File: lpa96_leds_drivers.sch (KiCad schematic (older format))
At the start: 115 parts, among them U3 TLC5941, U4 TLC5941, U5 TLC5941, U6 TLC5941, U7 TLC5941, U8 TLC5941

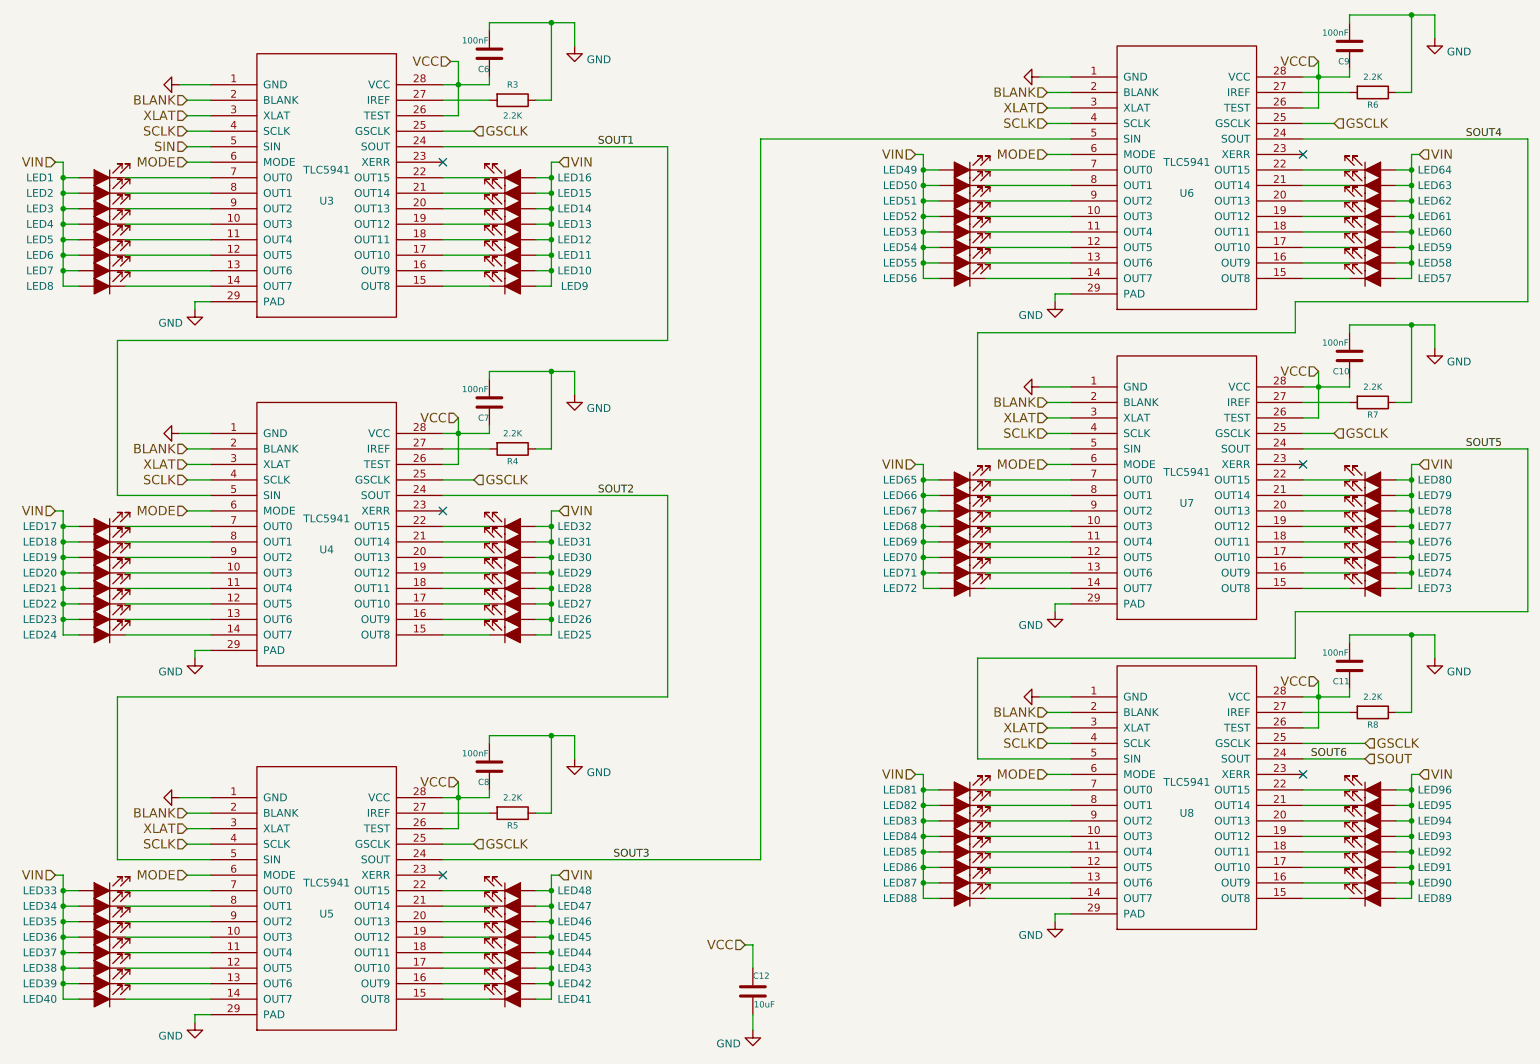
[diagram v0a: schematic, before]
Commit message: fix ERC errors, added last 3d model, other misc
changed TLC5941 pin29 pad to 'passive' type to fix ERC error
added PWR_FLAG special symbol on to input GND to fix ERC error
changed all VCC to proper power symbol instead of net alias
connected shield tabs of SDCARD footprint to GND (symbol doesn't have a pin)
changed SD_CARD symbol for pin8/9 are passive instead of NC (avoids ERCs)
changed name of pin8/9 from "RSV" to DAT1/DAT2 to match datasheet of guessed part
changed pin4 of regulator back to VCC (got messed up after change to VCC power symbols instead of net alias
added 3d model to P1 (revise after BOM received)
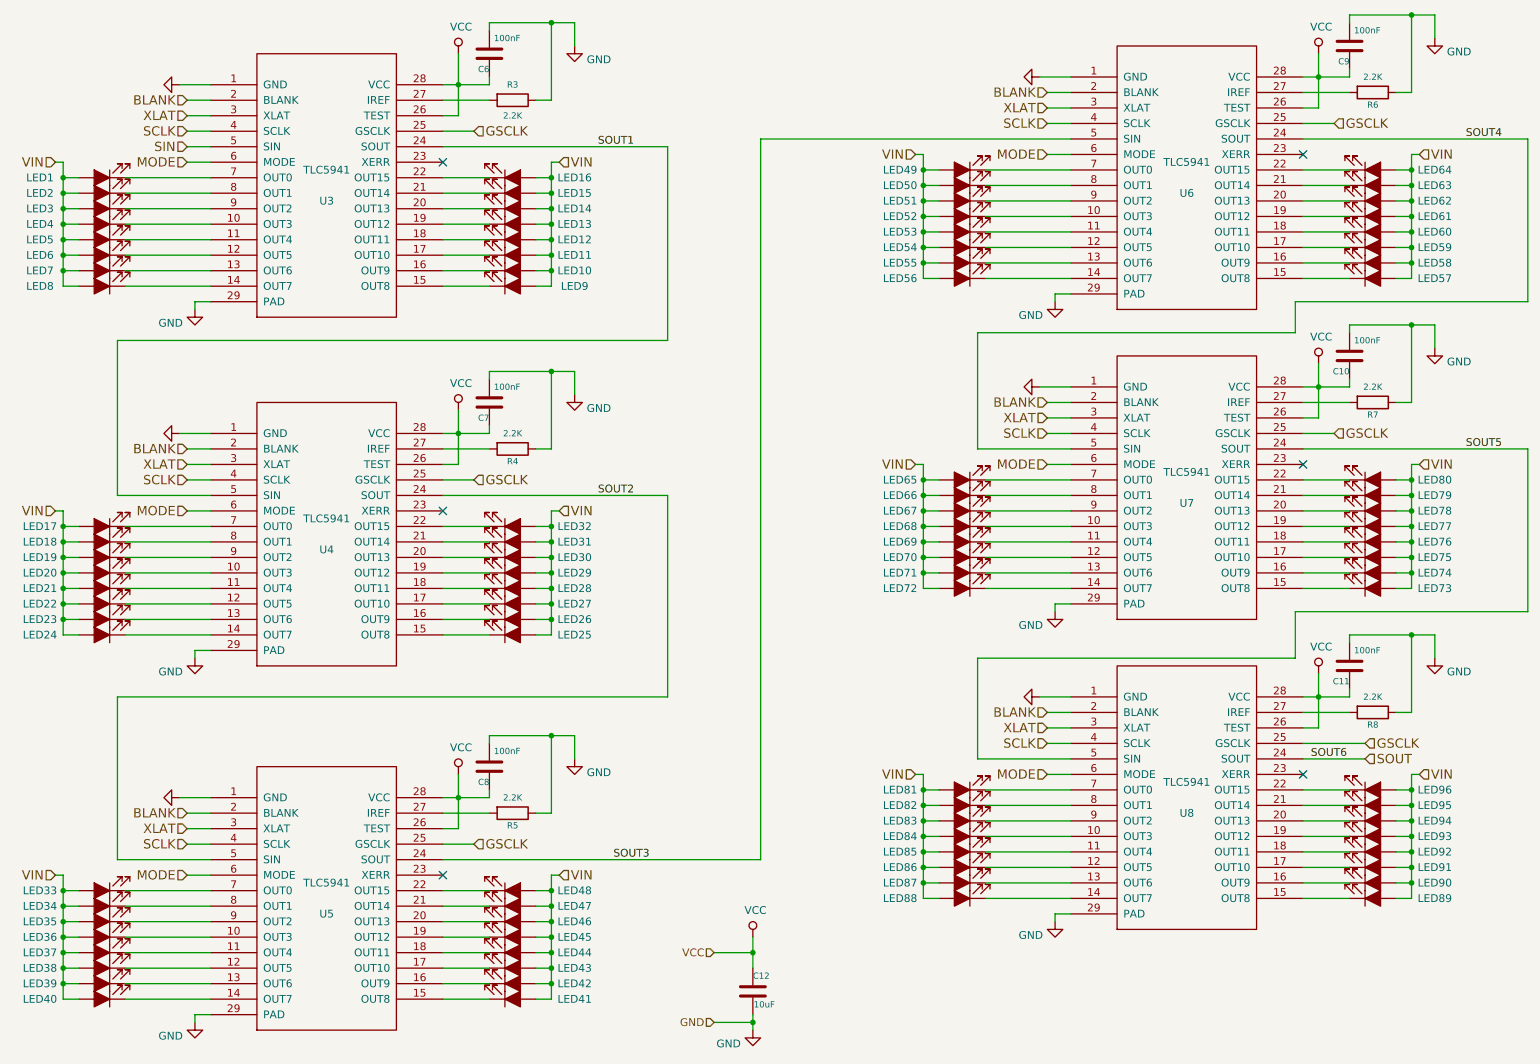
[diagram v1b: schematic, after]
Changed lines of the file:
@@
 EESchema Schematic File Version 4
-LIBS:tca-cache
+LIBS:lpa96-cache
 EELAYER 30 0
 EELAYER END
@@
 Connection ~ 3850 5600
 Wire Wire Line
-	3850 5500 3850 5600
-Wire Wire Line
 	3850 5800 3750 5800
 Wire Wire Line
@@
 	5200 1400 3750 1400
 Connection ~ 3850 3250
-Wire Wire Line
-	3850 3150 3850 3250
 Wire Wire Line
 	3850 3450 3750 3450
@@
 $EndComp
 $Comp
-L Device:C C8
-U 1 1 53630180
-P 4050 5400
-F 0 "C8" H 4050 5500 40  0000 L CNN
-F 1 "100nF" H 4056 5315 40  0000 L CNN
-F 2 "Capacitors_SMD:C_0805" H 4088 5250 30  0001 C CNN
-F 3 "~" H 4050 5400 60  0000 C CNN
-	1    4050 5400
-	-1   0    0    1
-$EndComp
-$Comp
 L lpa96_symbols:TLC5941 U4
 U 1 1 536301A0
@@
 	0    1    1    0
 $EndComp
-$Comp
-L Device:C C7
-U 1 1 53AA0807
-P 4050 3050
-F 0 "C7" H 4050 3150 40  0000 L CNN
-F 1 "100nF" H 4056 2965 40  0000 L CNN
-F 2 "Capacitors_SMD:C_0805" H 4088 2900 30  0001 C CNN
-F 3 "~" H 4050 3050 60  0000 C CNN
-	1    4050 3050
-	-1   0    0    1
-$EndComp
 NoConn ~ 3750 1500
 $Comp
@@
 $EndComp
 $Comp
-L Device:C C6
-U 1 1 53630972
-P 4050 800
-F 0 "C6" H 4050 900 40  0000 L CNN
-F 1 "100nF" H 4056 715 40  0000 L CNN
-F 2 "Capacitors_SMD:C_0805" H 4088 650 30  0001 C CNN
-F 3 "~" H 4050 800 60  0000 C CNN
-	1    4050 800
-	-1   0    0    1
-$EndComp
-$Comp
 L lpa96_symbols:TLC5941 U3
 U 1 1 53630973
@@
 Text HLabel 3950 5900 2    60   Input ~ 0
 GSCLK
-Text HLabel 3850 5500 0    60   Input ~ 0
-VCC
-Text HLabel 3850 3150 0    60   Input ~ 0
-VCC
 Text HLabel 4500 1500 2    60   Input ~ 0
 VIN
-Text HLabel 3800 850  0    60   Input ~ 0
-VCC
 Text HLabel 1250 1500 0    60   Input ~ 0
 VIN
@@
 Connection ~ 9400 4950
 Wire Wire Line
-	9400 4850 9400 4950
-Wire Wire Line
 	9400 5150 9300 5150
 Wire Wire Line
@@
 	9400 1150 9300 1150
 Connection ~ 9400 950
-Wire Wire Line
-	9400 850  9400 950
 Wire Wire Line
 	10000 1050 10000 550
@@
 	0    1    1    0
 $EndComp
-$Comp
-L Device:C C11
-U 1 1 53630EAA
-P 9600 4750
-F 0 "C11" H 9600 4850 40  0000 L CNN
-F 1 "100nF" H 9606 4665 40  0000 L CNN
-F 2 "Capacitors_SMD:C_0805" H 9638 4600 30  0001 C CNN
-F 3 "~" H 9600 4750 60  0000 C CNN
-	1    9600 4750
-	-1   0    0    1
-$EndComp
 NoConn ~ 9300 1450
 $Comp
@@
 $EndComp
 $Comp
-L Device:C C9
-U 1 1 53630EE2
-P 9600 750
-F 0 "C9" H 9600 850 40  0000 L CNN
-F 1 "100nF" H 9606 665 40  0000 L CNN
-F 2 "Capacitors_SMD:C_0805" H 9638 600 30  0001 C CNN
-F 3 "~" H 9600 750 60  0000 C CNN
-	1    9600 750
-	-1   0    0    1
-$EndComp
-$Comp
 L lpa96_symbols:TLC5941 U6
 U 1 1 53630EE8
@@
 Text HLabel 9700 5250 2    60   Input ~ 0
 GSCLK
-Text HLabel 9400 4850 0    60   Input ~ 0
-VCC
-Text HLabel 9400 850  0    60   Input ~ 0
-VCC
 Text HLabel 9700 5350 2    60   Input ~ 0
 SOUT
@@
 	2100 1100 2250 1100
 Wire Wire Line
-	3800 850  3850 850
-Wire Wire Line
-	3850 850  3850 1000
-Wire Wire Line
 	1300 4550 1400 4550
 Wire Wire Line
@@
 VIN
 Wire Wire Line
-	2050 5600 2250 5600
-Wire Wire Line
 	1300 6800 1300 6900
 Wire Wire Line
@@
 Wire Wire Line
 	9400 2950 9400 3150
-Text HLabel 9400 2850 0    60   Input ~ 0
-VCC
 Text HLabel 9500 3250 2    60   Input ~ 0
 GSCLK
-$Comp
-L Device:C C10
-U 1 1 53630EC9
-P 9600 2750
-F 0 "C10" H 9600 2850 40  0000 L CNN
-F 1 "100nF" H 9606 2665 40  0000 L CNN
-F 2 "Capacitors_SMD:C_0805" H 9638 2600 30  0001 C CNN
-F 3 "~" H 9600 2750 60  0000 C CNN
-	1    9600 2750
-	-1   0    0    1
-$EndComp
 $Comp
 L Device:R R7
@@
 $EndComp
 NoConn ~ 9300 3450
-$Comp
-L lpa96_symbols:TLC5941 U7
-U 1 1 53630EB0
-P 8550 3600
-F 0 "U7" H 8550 3500 50  0000 C CNN
-F 1 "TLC5941" H 8550 3700 50  0000 C CNN
-F 2 "lpa96_footprints:TLC5941_PWP_28" H 8550 3600 50  0001 C CNN
-F 3 "DOCUMENTATION" H 8550 3600 50  0001 C CNN
-	1    8550 3600
-	1    0    0    -1
-$EndComp
 Wire Wire Line
 	9600 2550 10000 2550
@@
 Wire Wire Line
 	9400 3150 9300 3150
-Wire Wire Line
-	9400 2850 9400 2950
 Connection ~ 9400 2950
 Wire Wire Line
@@
 	1    0    0    -1
 $EndComp
-Wire Wire Line
-	2250 7000 2150 7000
-Wire Wire Line
-	2150 7050 2150 7000
 $Comp
 L power:GND #PWR0105
@@
 	1    0    0    -1
 $EndComp
-Wire Wire Line
-	7800 2350 7700 2350
-Wire Wire Line
-	7700 2400 7700 2350
 $Comp
 L power:GND #PWR0106
@@
 	1    0    0    -1
 $EndComp
-Text HLabel 5700 6550 0    60   Input ~ 0
-VCC
-Wire Wire Line
-	5700 6550 5750 6550
 $Comp
 L power:GND #PWR0114
@@
 	9300 1050 9600 1050
 Wire Wire Line
-	5750 7000 5750 7100
-Wire Wire Line
-	5750 6550 5750 6700
+	5750 7000 5750 7050
 Wire Wire Line
 	4050 5200 4050 5250
@@
 	0    1    1    0
 $EndComp
+Wire Wire Line
+	2250 5600 2050 5600
+Wire Wire Line
+	2150 7050 2150 7000
+Wire Wire Line
+	2150 7000 2250 7000
+Wire Wire Line
+	7700 2400 7700 2350
+Wire Wire Line
+	7700 2350 7800 2350
+Text HLabel 5500 7050 0    50   Input ~ 0
+GND
+Wire Wire Line
+	5500 7050 5750 7050
+Connection ~ 5750 7050
+Wire Wire Line
+	5750 7050 5750 7100
+$Comp
+L lpa96_symbols:TLC5941 U7
+U 1 1 53630EB0
+P 8550 3600
+F 0 "U7" H 8550 3500 50  0000 C CNN
+F 1 "TLC5941" H 8550 3700 50  0000 C CNN
+F 2 "lpa96_footprints:TLC5941_PWP_28" H 8550 3600 50  0001 C CNN
+F 3 "DOCUMENTATION" H 8550 3600 50  0001 C CNN
+	1    8550 3600
+	1    0    0    -1
+$EndComp
+$Comp
+L power:VCC #PWR?
+U 1 1 5D9AE7D6
+P 9400 4800
+AR Path="/5D9AE7D6" Ref="#PWR?"  Part="1"
+AR Path="/5362FF20/5D9AE7D6" Ref="#PWR0126"  Part="1"
+F 0 "#PWR0126" H 9400 4650 50  0001 C CNN
+F 1 "VCC" H 9417 4973 50  0000 C CNN
+F 2 "" H 9400 4800 50  0001 C CNN
+F 3 "" H 9400 4800 50  0001 C CNN
+	1    9400 4800
+	1    0    0    -1
+$EndComp
+Wire Wire Line
+	9400 4800 9400 4950
+$Comp
+L Device:C C11
+U 1 1 53630EAA
+P 9600 4750
+F 0 "C11" H 9600 4850 40  0000 L CNN
+F 1 "100nF" H 9400 4650 40  0000 L CNN
+F 2 "Capacitors_SMD:C_0805" H 9638 4600 30  0001 C CNN
+F 3 "~" H 9600 4750 60  0000 C CNN
+	1    9600 4750
+	-1   0    0    1
+$EndComp
+$Comp
+L Device:C C10
+U 1 1 53630EC9
+P 9600 2750
+F 0 "C10" H 9600 2850 40  0000 L CNN
+F 1 "100nF" H 9400 2650 40  0000 L CNN
+F 2 "Capacitors_SMD:C_0805" H 9638 2600 30  0001 C CNN
+F 3 "~" H 9600 2750 60  0000 C CNN
+	1    9600 2750
+	-1   0    0    1
+$EndComp
+$Comp
+L power:VCC #PWR?
+U 1 1 5D9E9520
+P 9400 2800
+AR Path="/5D9E9520" Ref="#PWR?"  Part="1"
+AR Path="/5362FF20/5D9E9520" Ref="#PWR0127"  Part="1"
+F 0 "#PWR0127" H 9400 2650 50  0001 C CNN
+F 1 "VCC" H 9417 2973 50  0000 C CNN
+F 2 "" H 9400 2800 50  0001 C CNN
+F 3 "" H 9400 2800 50  0001 C CNN
+	1    9400 2800
+	1    0    0    -1
+$EndComp
+Wire Wire Line
+	9400 2800 9400 2950
+$Comp
+L Device:C C9
+U 1 1 53630EE2
+P 9600 750
+F 0 "C9" H 9600 850 40  0000 L CNN
+F 1 "100nF" H 9400 650 40  0000 L CNN
+F 2 "Capacitors_SMD:C_0805" H 9638 600 30  0001 C CNN
+F 3 "~" H 9600 750 60  0000 C CNN
+	1    9600 750
+	-1   0    0    1
+$EndComp
+$Comp
+L power:VCC #PWR?
+U 1 1 5DA231D4
+P 9400 800
+AR Path="/5DA231D4" Ref="#PWR?"  Part="1"
+AR Path="/5362FF20/5DA231D4" Ref="#PWR0128"  Part="1"
+F 0 "#PWR0128" H 9400 650 50  0001 C CNN
+F 1 "VCC" H 9417 973 50  0000 C CNN
+F 2 "" H 9400 800 50  0001 C CNN
+F 3 "" H 9400 800 50  0001 C CNN
+	1    9400 800
+	1    0    0    -1
+$EndComp
+Wire Wire Line
+	9400 800  9400 950
+$Comp
+L power:VCC #PWR?
+U 1 1 5DA5D878
+P 5750 6500
+AR Path="/5DA5D878" Ref="#PWR?"  Part="1"
+AR Path="/5362FF20/5DA5D878" Ref="#PWR0129"  Part="1"
+F 0 "#PWR0129" H 5750 6350 50  0001 C CNN
+F 1 "VCC" H 5767 6673 50  0000 C CNN
+F 2 "" H 5750 6500 50  0001 C CNN
+F 3 "" H 5750 6500 50  0001 C CNN
+	1    5750 6500
+	1    0    0    -1
+$EndComp
+$Comp
+L Device:C C8
+U 1 1 53630180
+P 4050 5400
+F 0 "C8" H 4050 5500 40  0000 L CNN
+F 1 "100nF" H 3850 5300 40  0000 L CNN
+F 2 "Capacitors_SMD:C_0805" H 4088 5250 30  0001 C CNN
+F 3 "~" H 4050 5400 60  0000 C CNN
+	1    4050 5400
+	-1   0    0    1
+$EndComp
+$Comp
+L power:VCC #PWR?
+U 1 1 5DB0D020
+P 3850 5450
+AR Path="/5DB0D020" Ref="#PWR?"  Part="1"
+AR Path="/5362FF20/5DB0D020" Ref="#PWR0130"  Part="1"
+F 0 "#PWR0130" H 3850 5300 50  0001 C CNN
+F 1 "VCC" H 3867 5623 50  0000 C CNN
+F 2 "" H 3850 5450 50  0001 C CNN
+F 3 "" H 3850 5450 50  0001 C CNN
+	1    3850 5450
+	1    0    0    -1
+$EndComp
+Wire Wire Line
+	3850 5450 3850 5600
+$Comp
+L Device:C C7
+U 1 1 53AA0807
+P 4050 3050
+F 0 "C7" H 4050 3150 40  0000 L CNN
+F 1 "100nF" H 3850 2950 40  0000 L CNN
+F 2 "Capacitors_SMD:C_0805" H 4088 2900 30  0001 C CNN
+F 3 "~" H 4050 3050 60  0000 C CNN
+	1    4050 3050
+	-1   0    0    1
+$EndComp
+$Comp
+L power:VCC #PWR?
+U 1 1 5DB46801
+P 3850 3100
+AR Path="/5DB46801" Ref="#PWR?"  Part="1"
+AR Path="/5362FF20/5DB46801" Ref="#PWR0131"  Part="1"
+F 0 "#PWR0131" H 3850 2950 50  0001 C CNN
+F 1 "VCC" H 3867 3273 50  0000 C CNN
+F 2 "" H 3850 3100 50  0001 C CNN
+F 3 "" H 3850 3100 50  0001 C CNN
+	1    3850 3100
+	1    0    0    -1
+$EndComp
+Wire Wire Line
+	3850 3100 3850 3250
+$Comp
+L Device:C C6
+U 1 1 53630972
+P 4050 800
+F 0 "C6" H 4050 900 40  0000 L CNN
+F 1 "100nF" H 3850 700 40  0000 L CNN
+F 2 "Capacitors_SMD:C_0805" H 4088 650 30  0001 C CNN
+F 3 "~" H 4050 800 60  0000 C CNN
+	1    4050 800
+	-1   0    0    1
+$EndComp
+$Comp
+L power:VCC #PWR?
+U 1 1 5DB7FF8C
+P 3850 800
+AR Path="/5DB7FF8C" Ref="#PWR?"  Part="1"
+AR Path="/5362FF20/5DB7FF8C" Ref="#PWR0132"  Part="1"
+F 0 "#PWR0132" H 3850 650 50  0001 C CNN
+F 1 "VCC" H 3867 973 50  0000 C CNN
+F 2 "" H 3850 800 50  0001 C CNN
+F 3 "" H 3850 800 50  0001 C CNN
+	1    3850 800
+	1    0    0    -1
+$EndComp
+Text HLabel 5500 6600 0    50   Input ~ 0
+VCC
+Wire Wire Line
+	5500 6600 5750 6600
+Connection ~ 5750 6600
+Wire Wire Line
+	5750 6600 5750 6700
+Wire Wire Line
+	3850 800  3850 1000
+Wire Wire Line
+	5750 6500 5750 6600
 $EndSCHEMATC
